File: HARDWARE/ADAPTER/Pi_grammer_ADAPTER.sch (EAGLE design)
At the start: 3 parts, among them J3 TESTBED, J4 CABLE

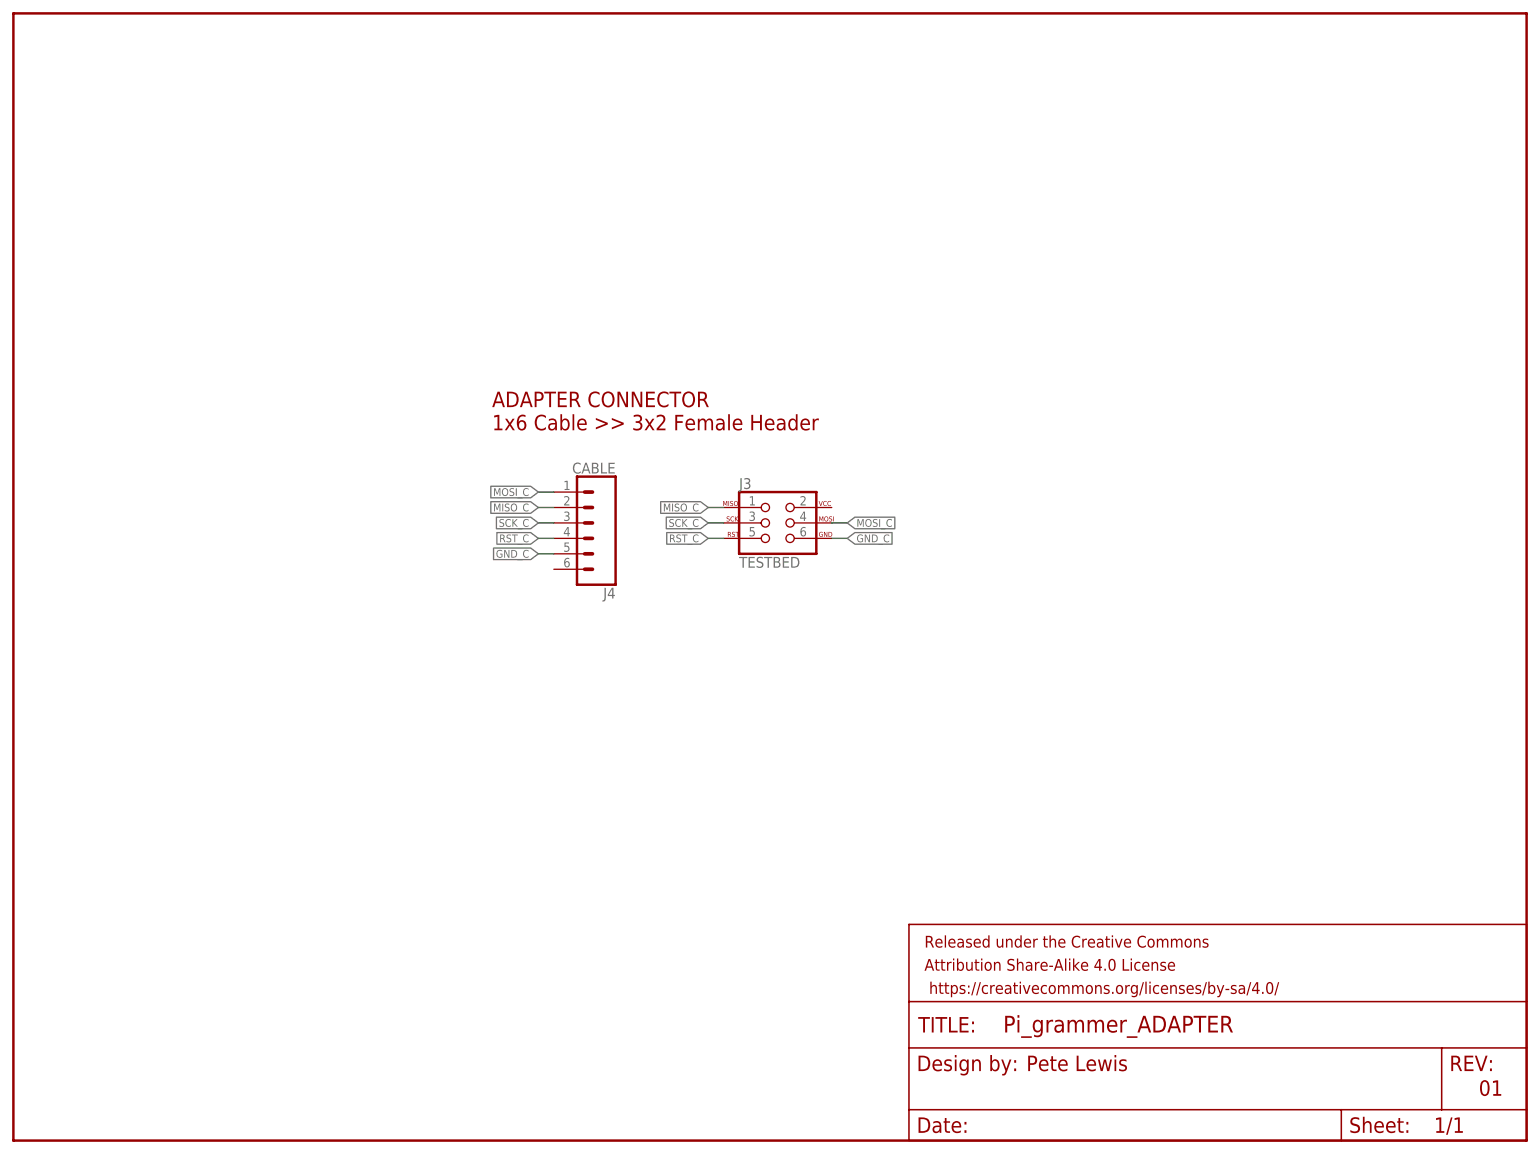
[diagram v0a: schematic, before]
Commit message: Option to "tap" logic level from target
Note, this required a modification to the ADAPTER as well. I am
utilizing pin 6 on the 1x6 pin header (jumper wire) to transfer VCC back
to the logic level converter.

I'm not sure why on the original design I didn't think to include VCC in
the comm lines to the target - I think it was because the raspi doesn't
have any ADCs to actually  verify it, so I didn't know if it was worth
it.
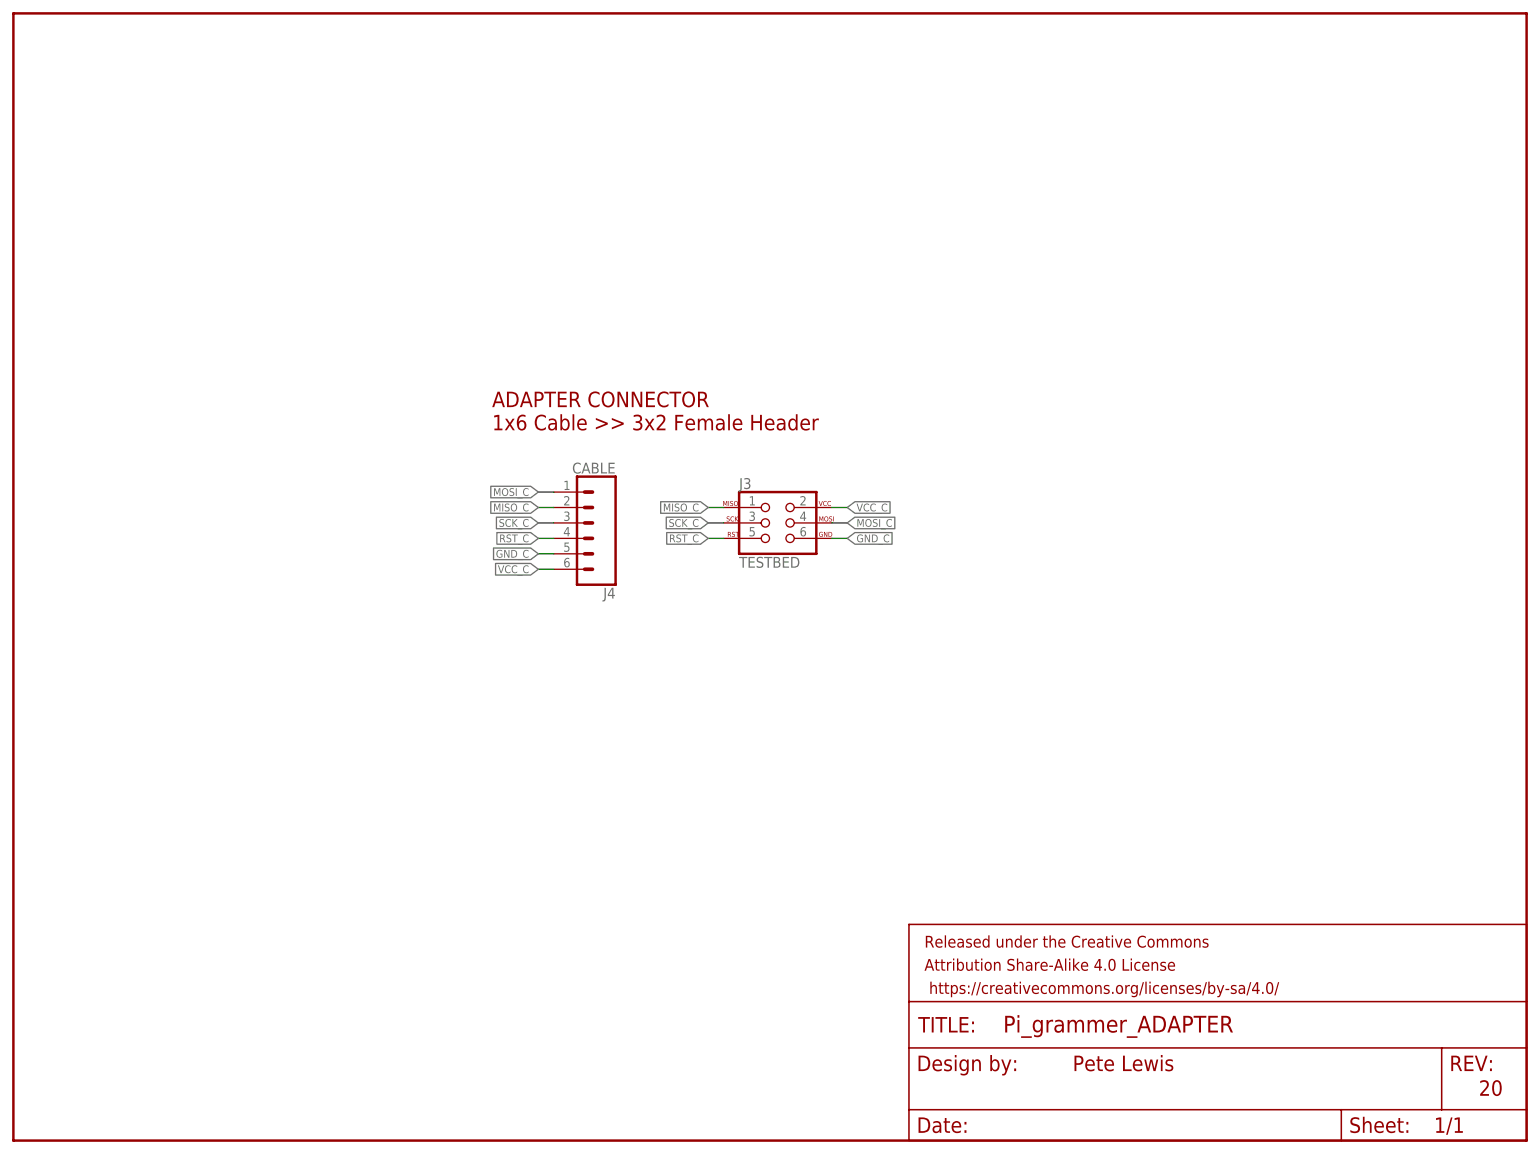
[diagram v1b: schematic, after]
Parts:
- J4: device SparkFun-Connectors:CONN_06RA -> SparkFun-Connectors:CONN_06RA_LOCK
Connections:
- new net VCC_C: J3.2, J4.6
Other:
- note added: "20"
- note removed: "01"
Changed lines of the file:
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@@
 <grid distance="0.1" unitdist="inch" unit="inch" style="lines" multiple="1" display="no" altdistance="0.01" altunitdist="inch" altunit="inch"/>
 <layers>
-<layer number="1" name="Top" color="4" fill="1" visible="no" active="no"/>
-<layer number="2" name="Route2" color="1" fill="3" visible="no" active="no"/>
-<layer number="3" name="Route3" color="4" fill="3" visible="no" active="no"/>
-<layer number="4" name="Route4" color="1" fill="4" visible="no" active="no"/>
-<layer number="5" name="Route5" color="4" fill="4" visible="no" active="no"/>
-<layer number="6" name="Route6" color="1" fill="8" visible="no" active="no"/>
-<layer number="7" name="Route7" color="4" fill="8" visible="no" active="no"/>
-<layer number="8" name="Route8" color="1" fill="2" visible="no" active="no"/>
-<layer number="9" name="Route9" color="4" fill="2" visible="no" active="no"/>
-<layer number="10" name="Route10" color="1" fill="7" visible="no" active="no"/>
-<layer number="11" name="Route11" color="4" fill="7" visible="no" active="no"/>
-<layer number="12" name="Route12" color="1" fill="5" visible="no" active="no"/>
-<layer number="13" name="Route13" color="4" fill="5" visible="no" active="no"/>
-<layer number="14" name="Route14" color="1" fill="6" visible="no" active="no"/>
-<layer number="15" name="Route15" color="4" fill="6" visible="no" active="no"/>
-<layer number="16" name="Bottom" color="1" fill="1" visible="no" active="no"/>
-<layer number="17" name="Pads" color="2" fill="1" visible="no" active="no"/>
-<layer number="18" name="Vias" color="2" fill="1" visible="no" active="no"/>
-<layer number="19" name="Unrouted" color="6" fill="1" visible="no" active="no"/>
-<layer number="20" name="Dimension" color="15" fill="1" visible="no" active="no"/>
-<layer number="21" name="tPlace" color="16" fill="1" visible="no" active="no"/>
-<layer number="22" name="bPlace" color="14" fill="1" visible="no" active="no"/>
-<layer number="23" name="tOrigins" color="15" fill="1" visible="no" active="no"/>
-<layer number="24" name="bOrigins" color="15" fill="1" visible="no" active="no"/>
-<layer number="25" name="tNames" color="7" fill="1" visible="no" active="no"/>
-<layer number="26" name="bNames" color="7" fill="1" visible="no" active="no"/>
-<layer number="27" name="tValues" color="7" fill="1" visible="no" active="no"/>
-<layer number="28" name="bValues" color="7" fill="1" visible="no" active="no"/>
+<layer number="1" name="Top" color="4" fill="1" visible="yes" active="no"/>
+<layer number="2" name="Route2" color="1" fill="3" visible="yes" active="no"/>
+<layer number="3" name="Route3" color="4" fill="3" visible="yes" active="no"/>
+<layer number="4" name="Route4" color="1" fill="4" visible="yes" active="no"/>
+<layer number="5" name="Route5" color="4" fill="4" visible="yes" active="no"/>
+<layer number="6" name="Route6" color="1" fill="8" visible="yes" active="no"/>
+<layer number="7" name="Route7" color="4" fill="8" visible="yes" active="no"/>
+<layer number="8" name="Route8" color="1" fill="2" visible="yes" active="no"/>
+<layer number="9" name="Route9" color="4" fill="2" visible="yes" active="no"/>
+<layer number="10" name="Route10" color="1" fill="7" visible="yes" active="no"/>
+<layer number="11" name="Route11" color="4" fill="7" visible="yes" active="no"/>
+<layer number="12" name="Route12" color="1" fill="5" visible="yes" active="no"/>
+<layer number="13" name="Route13" color="4" fill="5" visible="yes" active="no"/>
+<layer number="14" name="Route14" color="1" fill="6" visible="yes" active="no"/>
+<layer number="15" name="Route15" color="4" fill="6" visible="yes" active="no"/>
+<layer number="16" name="Bottom" color="1" fill="1" visible="yes" active="no"/>
+<layer number="17" name="Pads" color="2" fill="1" visible="yes" active="no"/>
+<layer number="18" name="Vias" color="2" fill="1" visible="yes" active="no"/>
+<layer number="19" name="Unrouted" color="6" fill="1" visible="yes" active="no"/>
+<layer number="20" name="Dimension" color="15" fill="1" visible="yes" active="no"/>
+<layer number="21" name="tPlace" color="16" fill="1" visible="yes" active="no"/>
+<layer number="22" name="bPlace" color="14" fill="1" visible="yes" active="no"/>
+<layer number="23" name="tOrigins" color="15" fill="1" visible="yes" active="no"/>
+<layer number="24" name="bOrigins" color="15" fill="1" visible="yes" active="no"/>
+<layer number="25" name="tNames" color="7" fill="1" visible="yes" active="no"/>
+<layer number="26" name="bNames" color="7" fill="1" visible="yes" active="no"/>
+<layer number="27" name="tValues" color="7" fill="1" visible="yes" active="no"/>
+<layer number="28" name="bValues" color="7" fill="1" visible="yes" active="no"/>
 <layer number="29" name="tStop" color="7" fill="3" visible="no" active="no"/>
 <layer number="30" name="bStop" color="7" fill="6" visible="no" active="no"/>
@@
 <layer number="35" name="tGlue" color="7" fill="4" visible="no" active="no"/>
 <layer number="36" name="bGlue" color="7" fill="5" visible="no" active="no"/>
-<layer number="37" name="tTest" color="7" fill="1" visible="no" active="no"/>
-<layer number="38" name="bTest" color="7" fill="1" visible="no" active="no"/>
+<layer number="37" name="tTest" color="7" fill="1" visible="yes" active="no"/>
+<layer number="38" name="bTest" color="7" fill="1" visible="yes" active="no"/>
 <layer number="39" name="tKeepout" color="4" fill="11" visible="no" active="no"/>
 <layer number="40" name="bKeepout" color="1" fill="11" visible="no" active="no"/>
@@
 <layer number="44" name="Drills" color="7" fill="1" visible="no" active="no"/>
 <layer number="45" name="Holes" color="7" fill="1" visible="no" active="no"/>
-<layer number="46" name="Milling" color="3" fill="1" visible="no" active="no"/>
-<layer number="47" name="Measures" color="7" fill="1" visible="no" active="no"/>
-<layer number="48" name="Document" color="7" fill="1" visible="no" active="no"/>
-<layer number="49" name="Reference" color="7" fill="1" visible="no" active="no"/>
-<layer number="50" name="dxf" color="7" fill="1" visible="no" active="no"/>
-<layer number="51" name="tDocu" color="6" fill="1" visible="no" active="no"/>
-<layer number="52" name="bDocu" color="7" fill="1" visible="no" active="no"/>
-<layer number="53" name="tGND_GNDA" color="7" fill="9" visible="no" active="no"/>
-<layer number="54" name="bGND_GNDA" color="1" fill="9" visible="no" active="no"/>
-<layer number="56" name="wert" color="7" fill="1" visible="no" active="no"/>
-<layer number="57" name="tCAD" color="7" fill="1" visible="no" active="no"/>
-<layer number="59" name="tCarbon" color="7" fill="1" visible="no" active="no"/>
-<layer number="60" name="bCarbon" color="7" fill="1" visible="no" active="no"/>
+<layer number="46" name="Milling" color="3" fill="1" visible="yes" active="no"/>
+<layer number="47" name="Measures" color="7" fill="1" visible="yes" active="no"/>
+<layer number="48" name="Document" color="7" fill="1" visible="yes" active="no"/>
+<layer number="49" name="Reference" color="7" fill="1" visible="yes" active="no"/>
+<layer number="50" name="dxf" color="7" fill="1" visible="yes" active="no"/>
+<layer number="51" name="tDocu" color="6" fill="1" visible="yes" active="no"/>
+<layer number="52" name="bDocu" color="7" fill="1" visible="yes" active="no"/>
+<layer number="53" name="tGND_GNDA" color="7" fill="9" visible="yes" active="no"/>
+<layer number="54" name="bGND_GNDA" color="1" fill="9" visible="yes" active="no"/>
+<layer number="56" name="wert" color="7" fill="1" visible="yes" active="no"/>
+<layer number="57" name="tCAD" color="7" fill="1" visible="yes" active="no"/>
+<layer number="59" name="tCarbon" color="7" fill="1" visible="yes" active="no"/>
+<layer number="60" name="bCarbon" color="7" fill="1" visible="yes" active="no"/>
 <layer number="90" name="Modules" color="5" fill="1" visible="yes" active="yes"/>
 <layer number="91" name="Nets" color="2" fill="1" visible="yes" active="yes"/>
@@
 <attribute name="PROD_ID" value="CONN-11566"/>
 </part>
-<part name="J4" library="SparkFun-Connectors" deviceset="CONN_06" device="RA" value="CABLE">
+<part name="J4" library="SparkFun-Connectors" deviceset="CONN_06" device="RA_LOCK" value="CABLE">
 <attribute name="PROD_ID" value="CONN-10140"/>
 </part>
@@
 <text x="86.36" y="299.72" size="2.54" layer="94" font="vector">ADAPTER CONNECTOR
 1x6 Cable &gt;&gt; 3x2 Female Header</text>
-<text x="174.244" y="194.31" size="2.54" layer="94" font="vector">Pete Lewis</text>
-<text x="248.666" y="190.246" size="2.54" layer="94" font="vector">01</text>
+<text x="181.864" y="194.31" size="2.54" layer="94" font="vector">Pete Lewis</text>
+<text x="248.666" y="190.246" size="2.54" layer="94" font="vector">20</text>
 </plain>
 <instances>
@@
 </segment>
 </net>
+<net name="VCC_C" class="0">
+<segment>
+<pinref part="J3" gate="G$1" pin="2"/>
+<wire x1="142.24" y1="287.02" x2="144.78" y2="287.02" width="0.1524" layer="91"/>
+<label x="144.78" y="287.02" size="1.27" layer="95" xref="yes"/>
+</segment>
+<segment>
+<pinref part="J4" gate="G$1" pin="6"/>
+<wire x1="96.52" y1="276.86" x2="93.98" y2="276.86" width="0.1524" layer="91"/>
+<label x="93.98" y="276.86" size="1.27" layer="95" rot="R180" xref="yes"/>
+</segment>
+</net>
